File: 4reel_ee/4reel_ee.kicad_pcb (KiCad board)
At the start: 4 copper layers, 118 x 30 mm, 141 parts, among them J1 USB_C_Receptacle_USB2.0_16P, J2 Micro_SD_Card_Det2, J3 RJ45_Hanrun_HR911105A_Horizon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, J4 JST, U1 RV1103G, U2 EA3036C, U3 ImageSensor_OV9281, U4 TLV73312PDBV, U5 TPD2EUSB30, U6 TLV73328PDBV, U7 W25Q16JVSS, U8 LIS2HH12, U9 ImageSensor_OV9281, Y1 TXC-7C, Y2 24Mhz, Y3 TXC-7C

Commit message: Worked on the routing
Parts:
- removed R26, R27, R28, R29: 49.9R, Resistor_SMD:R_0402_1005Metric
- added C73: 10nF, Capacitor_SMD:C_0402_1005Metric, F.Cu at (110.5, 92.7)
- added C74: 10nF, Capacitor_SMD:C_0402_1005Metric, F.Cu at (109.1, 99.0)
- added C75: 100nF, Capacitor_SMD:C_0402_1005Metric, B.Cu at (124.2, 100.9)
- C17, C19, C21, C24, C27, C28, C37, C72: moved to B.Cu
- R16: moved to F.Cu
- U7: value W25Q16JVSS -> W25Q32JVZP; footprint Package_SO:SOIC-8_5.3x5.3mm_P1.27mm -> Package_SON:WSON-8-1EP_6x5mm_P1.27mm_EP3.4x4.3mm
- moved C54 115.5 mm to (119.0, 103.6), turned to 90 degrees
- moved C49 113.4 mm to (120.1, 103.6), turned to 90 degrees
- moved R22 110.3 mm to (122.2, 105.8), turned to 0 degrees
- moved U8 110.0 mm to (122.0, 104.0), turned to 180 degrees
- moved R21 108.7 mm to (122.2, 102.1), turned to 0 degrees
- moved U7 85.8 mm to (137.9, 106.2), turned to 180 degrees
- moved R30 60.1 mm to (107.9, 108.4), turned to 180 degrees
- moved R31 55.1 mm to (111.9, 108.4), turned to 0 degrees
- moved D1 28.4 mm to (118.2, 96.1), turned to 90 degrees
- moved D2 27.3 mm to (119.2, 96.1), turned to 90 degrees
- moved R23 26.7 mm to (118.2, 98.0), turned to -90 degrees
- moved R24 25.6 mm to (119.2, 98.0), turned to -90 degrees
- moved C72 9.78 mm to (122.5, 91.4), turned to 180 degrees
- moved C50 9.44 mm to (146.0, 96.8), turned to 0 degrees
- moved R11 8.89 mm to (108.7, 90.0)
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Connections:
- J3 pad 4: +3V3 -> Net-(J3-TCT)
- J3 pad 5: +3V3 -> Net-(J3-RCT)
- U1 pad 60: /MPU/STROBE1 -> /MPU/STROBE2
- U1 pad 61: /MPU/VSYNC1 -> /MPU/VSYNC2
- U1 pad 64: /MPU/XSHUTDOWN1 -> /MPU/XSHUTDOWN2
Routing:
- net +3V3: track 16.6 -> 139.4 mm, vias 1 -> 9
- net /MPU/I2C4.SDA: track 14.7 -> 81.9 mm, vias 0 -> 2
- net /MPU/I2C4.SCL: track 22.5 -> 89.7 mm, vias 0 -> 2
- net +5V: track 9.92 -> 58.0 mm
- net +1V8: track 8.95 -> 55.5 mm, vias 0 -> 6
- net /MPU/VSYNC2: track 0.69 -> 41.1 mm, vias 0 -> 1
- net /MPU/XSHUTDOWN2: track 2.39 -> 42.1 mm, vias 0 -> 1
- net /MPU/STROBE2: track 1.15 -> 40.5 mm, vias 0 -> 1
- net +0V9: track 0.00 -> 33.1 mm, vias 0 -> 6
- net /MPU/EPHY.RXN: track 0.00 -> 25.4 mm
- net /MPU/EPHY.RXP: track 0.00 -> 25.3 mm
- net /MPU/SDMMC.CLK: track 0.11 -> 23.7 mm, vias 0 -> 1
- net /MPU/EPHY.TXN: track 0.00 -> 23.4 mm
- net /MPU/EPHY.TXP: track 0.00 -> 23.2 mm
- net /Flash/FSPI.~{CS}: track 0.00 -> 21.6 mm, vias 0 -> 1
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
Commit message: Worked on the routing.
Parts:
- C35, C46, C58, C63, C67, C68, C71: moved to F.Cu
- moved C31 93.4 mm to (135.2, 110.0), turned to -90 degrees
- moved R18 90.2 mm to (134.0, 105.7), turned to 90 degrees
- moved R17 85.4 mm to (138.5, 103.0)
- moved C35 5.40 mm to (162.9, 95.7)
- moved C46 5.30 mm to (162.9, 94.7)
- moved C58 4.73 mm to (90.9, 94.4)
- moved C53 3.30 mm to (165.4, 91.2), turned to 90 degrees
- moved C63 3.02 mm to (90.9, 91.4), turned to 0 degrees
- moved R31 2.82 mm to (113.8, 110.5), turned to 90 degrees
- moved TP1 2.60 mm to (160.3, 107.4)
- moved TP2 2.55 mm to (157.8, 107.4)
- moved C66 2.24 mm to (88.9, 98.2), turned to -90 degrees
- moved C69 2.15 mm to (89.9, 98.2), turned to -90 degrees
- moved C71 2.14 mm to (90.9, 95.4)
- moved C48 1.58 mm to (166.8, 100.8), turned to 0 degrees
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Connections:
- J4 pad 2: /MPU/UART_RX -> /MPU/UART_TX
- J4 pad 3: /MPU/UART_TX -> /MPU/UART_RX
- U1 pad 52: unconnected-(U1GPIO / Peripherals-PWM10_M1-Pad52) -> /LED100
- U1 pad 57: unconnected-(U1GPIO / Peripherals-PWM3_IR_M2-Pad57) -> /LED_ACT
- U1 pad 61: /MPU/VSYNC2 -> /MPU/VSYNC
- U1 pad 64: /MPU/XSHUTDOWN2 -> /MPU/XSHUTDOWN
- U1 pad 65: unconnected-(U1GPIO / Peripherals-PWM2_M2-Pad65) -> /MPU/STROBE1
- U3 pad A5: /MPU/XSHUTDOWN1 -> /MPU/XSHUTDOWN
- U3 pad B5: /MPU/VSYNC1 -> /MPU/VSYNC
- U3 pad E1: +1V8 -> /OV9281/DVDD
- U9 pad A5: /MPU/XSHUTDOWN2 -> /MPU/XSHUTDOWN
- U9 pad B5: /MPU/VSYNC2 -> /MPU/VSYNC
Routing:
- net +1V8: track 55.5 -> 186.4 mm, vias 6 -> 11
- net +1V2: track 1.36 -> 125.5 mm, vias 0 -> 3
- net +2V8: track 4.51 -> 120.3 mm, vias 0 -> 4
- net /MPU/VSYNC: track 0.00 -> 91.5 mm, vias 0 -> 3
- net /MPU/XSHUTDOWN: track 0.00 -> 91.3 mm, vias 0 -> 1
- net +0V9: track 33.1 -> 100.4 mm, vias 6 -> 8
- net /MPU/STROBE1: track 2.19 -> 53.3 mm, vias 0 -> 1
- net /MPU/UART_TX: track 0.71 -> 44.8 mm, vias 1 -> 2
- net +5V: track 58.0 -> 100.4 mm, vias 2 -> 5
- net /MPU/XSHUTDOWN2: track 42.1 -> 0.00 mm, vias 1 -> 0
- net /MPU/UART_RX: track 0.77 -> 41.9 mm, vias 1 -> 2
- net /MPU/VSYNC2: track 41.1 -> 0.00 mm, vias 1 -> 0
- net +3V3: track 139.4 -> 180.1 mm, vias 9 -> 13
- net /LED_ACT: track 0.00 -> 27.8 mm, vias 0 -> 1
- net /LED100: track 0.00 -> 24.5 mm, vias 0 -> 1
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
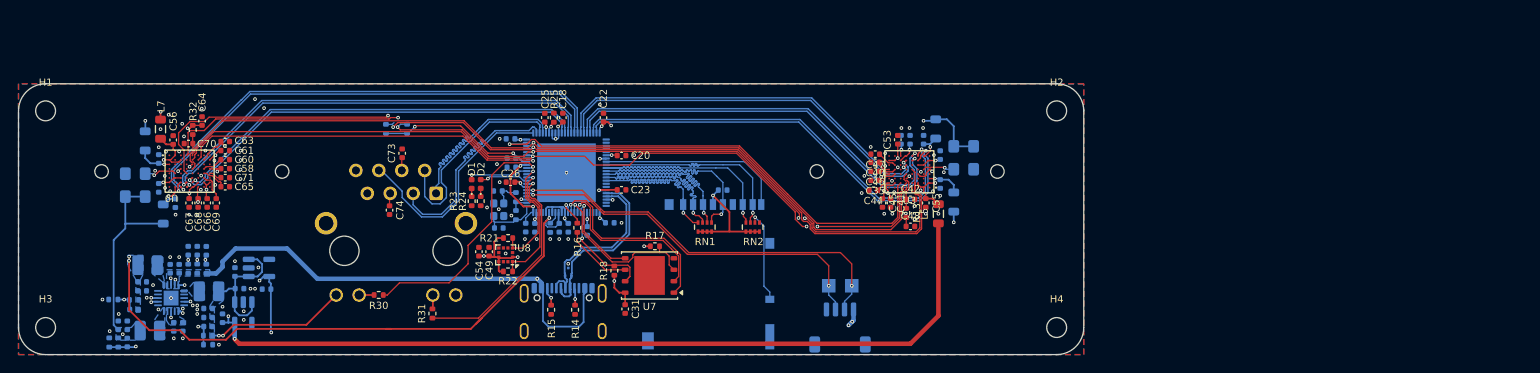
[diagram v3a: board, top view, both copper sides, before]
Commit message: Finished initial rough layout.
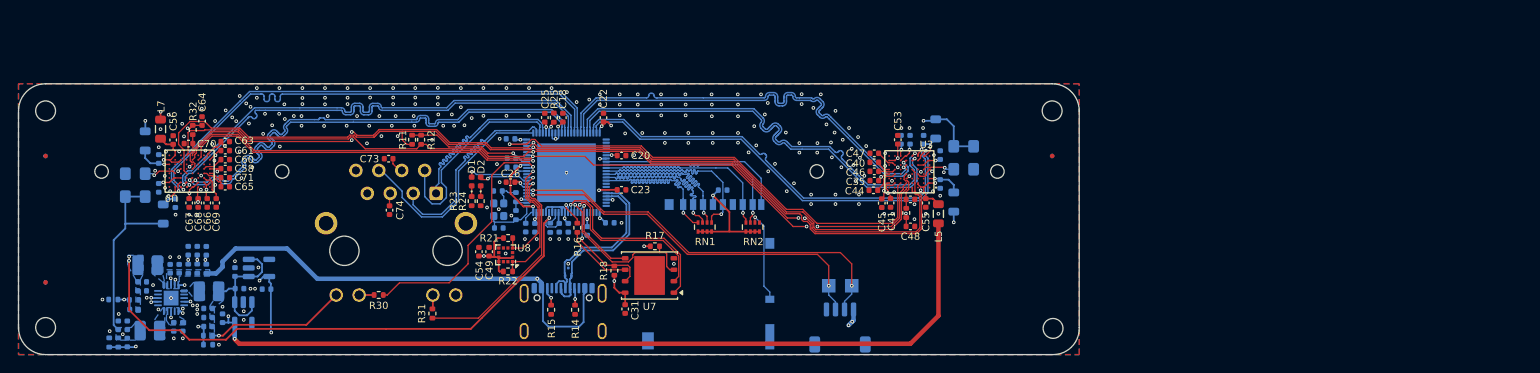
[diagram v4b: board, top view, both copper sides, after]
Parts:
- added FID1: Fiducial, Fiducial:Fiducial_0.5mm_Mask1.5mm, F.Cu at (71.0, 93.0)
- added FID2: Fiducial, Fiducial:Fiducial_0.5mm_Mask1.5mm, B.Cu at (71.0, 107.0)
- added FID3: Fiducial, Fiducial:Fiducial_0.5mm_Mask1.5mm, F.Cu at (71.0, 107.0)
- added FID4: Fiducial, Fiducial:Fiducial_0.5mm_Mask1.5mm, F.Cu at (182.5, 93.0)
- added FID5: Fiducial, Fiducial:Fiducial_0.5mm_Mask1.5mm, B.Cu at (71.0, 93.0)
- added FID6: Fiducial, Fiducial:Fiducial_0.5mm_Mask1.5mm, B.Cu at (182.5, 93.0)
- R11, R12: moved to F.Cu
- moved R11 3.14 mm to (111.6, 91.2), turned to -90 degrees
- moved R12 1.97 mm to (112.6, 91.2), turned to -90 degrees
- moved C73 1.62 mm to (109.0, 93.3), turned to 180 degrees
- moved H2 0.50 mm to (182.5, 88.0)
- moved H4 0.41 mm to (182.6, 112.1)
- moved D1 0.28 mm to (118.2, 95.8)
- moved D2 0.27 mm to (119.2, 95.8)
- moved C47 0.14 mm to (162.8, 92.7)
- moved C40 0.11 mm to (162.8, 93.7)
- moved C35 0.10 mm to (162.8, 95.7)
- moved C46 0.10 mm to (162.8, 94.7)
- moved C45 0.08 mm to (163.6, 98.2)
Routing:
- net /MPU/MIPI2.D1P: track 46.6 -> 53.2 mm
- net /MPU/MIPI2.D1N: track 46.9 -> 53.2 mm
- net /MPU/MIPI1.D1N: track 43.4 -> 47.9 mm
- net /MPU/MIPI1.D1P: track 44.0 -> 47.9 mm
- net +1V8: track 186.4 -> 182.7 mm, vias 11 -> 10
- net /MPU/MIPI2.CK0N: track 49.8 -> 53.3 mm
- net /MPU/MIPI1.CK0N: track 46.3 -> 49.4 mm
- net /MPU/I2C4.SDA: track 99.5 -> 96.6 mm, vias 5 -> 3
- net /MPU/MIPI1.CK0P: track 45.1 -> 48.0 mm
- net +3V3: track 180.1 -> 177.3 mm, vias 13 -> 11
- net /MPU/MIPI2.CK0P: track 50.9 -> 53.7 mm
- net +0V9: track 100.4 -> 98.2 mm
- net /MPU/VSYNC: track 91.5 -> 89.7 mm
- net /MPU/SDMMC.D0: track 24.5 -> 22.8 mm
- net /MPU/MIPI2.D0N: track 55.4 -> 56.6 mm
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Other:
- board size 118 x 30 mm -> 117.5 x 30 mm

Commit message: R0.1-rc1
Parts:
- added R26: 10k, Resistor_SMD:R_0402_1005Metric, F.Cu at (134.8, 96.3)
- added R27: 22R, Resistor_SMD:R_0201_0603Metric, B.Cu at (135.0, 94.4)
- moved C23 0.55 mm to (134.8, 97.3)
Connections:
- J2 pad 10: Net-(J2-DET_A) -> GND
- RN1 pad 1: /MPU/SDMMC.CLK -> unconnected-(RN1-R1.1-Pad1)
- RN2 pad 1: unconnected-(RN2-R1.1-Pad1) -> /MPU/SDMMC.DET
- RN2 pad 2: Net-(J2-DET_A) -> unconnected-(RN2-R2.1-Pad2)
- U1 pad 11: /MPU/SDMMC.CLK -> Net-(U1GPIO / Peripherals-SDMMC_CLK)
- U1 pad 16: unconnected-(U1Analog / High-Speed-SARADC_IN0-Pad16) -> Net-(U1Analog / High-Speed-SARADC_IN0)
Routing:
- net Net-(J2-DET_A): track 10.4 -> 0.00 mm, vias 1 -> 0
- net /MPU/MIPI2.D1P: track 53.2 -> 56.4 mm
- net /MPU/MIPI2.D1N: track 53.2 -> 56.4 mm
- net /MPU/MIPI2.CK0P: track 53.7 -> 56.9 mm
- net /MPU/MIPI2.CK0N: track 53.3 -> 56.5 mm
- net /MPU/SDMMC.CLK: track 23.7 -> 21.2 mm, vias 1 -> 0
- net /MPU/SDMMC.DET: track 20.8 -> 23.2 mm, vias 0 -> 1
- net Net-(U1GPIO / Peripherals-SDMMC_CLK): track 0.00 -> 1.69 mm
- net +1V8: track 182.7 -> 184.4 mm
- net /MPU/MIPI1.D1N: track 47.9 -> 49.3 mm
- net /MPU/MIPI1.D1P: track 47.9 -> 49.3 mm
- net /MPU/MIPI1.CK0P: track 48.0 -> 49.4 mm
- net Net-(U1Analog / High-Speed-SARADC_IN0): track 0.00 -> 1.24 mm, vias 0 -> 1
- net /MPU/MIPI1.D0P: track 48.1 -> 49.1 mm
- net /MPU/MIPI1.D0N: track 48.1 -> 49.2 mm
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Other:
- board text added: "100 OHM Controlled Impedance"
- board text added: "90 OHM Controlled impedance"

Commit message: R0.1 release.
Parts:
- added TP3: TestPoint, TestPoint:TestPoint_Pad_1.0x1.0mm, F.Cu at (110.1, 91.2)
- added TP4: TestPoint, TestPoint:TestPoint_Pad_1.0x1.0mm, F.Cu at (107.7, 91.7)
- added TP5: TestPoint, TestPoint:TestPoint_Pad_1.0x1.0mm, F.Cu at (124.3, 105.0)
- added TP6: TestPoint, TestPoint:TestPoint_Pad_1.0x1.0mm, F.Cu at (124.3, 103.0)
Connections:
- C35 pad 1: /OV9281/DOVDD -> /OV9281/DVDD
- C36 pad 1: /OV9281/DOVDD -> /OV9281/DVDD
- C39 pad 1: /OV9281/DVDD -> /OV9281/DOVDD
- C41 pad 1: /OV9281/DVDD -> /OV9281/DOVDD
- C51 pad 1: /OV9281/DVDD -> /OV9281/DOVDD
- C52 pad 1: /OV9281/DOVDD -> /OV9281/DVDD
- C55 pad 1: /OV9281/DOVDD -> /OV9281/DVDD
- C56 pad 1: /OV9282/DOVDD -> /OV9282/DVDD
- C58 pad 1: /OV9282/DOVDD -> /OV9282/DVDD
- C59 pad 1: /OV9282/DVDD -> /OV9282/DOVDD
- C62 pad 1: /OV9282/DOVDD -> /OV9282/DVDD
- C63 pad 1: /OV9282/DVDD -> /OV9282/DOVDD
- C67 pad 1: /OV9282/DOVDD -> /OV9282/DVDD
- C68 pad 1: /OV9282/DVDD -> /OV9282/DOVDD
- L5 pad 2: /OV9281/DOVDD -> /OV9281/DVDD
- L6 pad 2: /OV9281/DVDD -> /OV9281/DOVDD
- L7 pad 2: /OV9282/DOVDD -> /OV9282/DVDD
- L9 pad 2: /OV9282/DVDD -> /OV9282/DOVDD
- U3 pad A2: /OV9281/DOVDD -> /OV9281/DVDD
- U3 pad B1: /OV9281/DOVDD -> /OV9281/DVDD
- U3 pad B3: /OV9281/DOVDD -> /OV9281/DVDD
- U3 pad B7: /OV9281/DVDD -> /OV9281/DOVDD
- U3 pad C5: /OV9281/DOVDD -> /OV9281/DVDD
- U3 pad D3: /OV9281/DVDD -> /OV9281/DOVDD
- U3 pad D8: /OV9281/DOVDD -> /OV9281/DVDD
- U3 pad E1: /OV9281/DVDD -> /OV9281/DOVDD
- U3 pad F2: /OV9281/DOVDD -> /OV9281/DVDD
- U3 pad F3: /OV9281/DOVDD -> /OV9281/DVDD
- U3 pad G1: /OV9281/DOVDD -> /OV9281/DVDD
- U3 pad G6: /OV9281/DOVDD -> /OV9281/DVDD
- U3 pad H2: /OV9281/DVDD -> /OV9281/DOVDD
- U3 pad H5: /OV9281/DOVDD -> /OV9281/DVDD
- U3 pad H6: /OV9281/DVDD -> /OV9281/DOVDD
- U9 pad A2: /OV9282/DOVDD -> /OV9282/DVDD
- U9 pad B1: /OV9282/DOVDD -> /OV9282/DVDD
- U9 pad B3: /OV9282/DOVDD -> /OV9282/DVDD
- U9 pad B7: /OV9282/DVDD -> /OV9282/DOVDD
- U9 pad C5: /OV9282/DOVDD -> /OV9282/DVDD
- U9 pad D3: /OV9282/DVDD -> /OV9282/DOVDD
- U9 pad D8: /OV9282/DOVDD -> /OV9282/DVDD
- U9 pad F2: /OV9282/DOVDD -> /OV9282/DVDD
- U9 pad F3: /OV9282/DOVDD -> /OV9282/DVDD
- U9 pad G1: /OV9282/DOVDD -> /OV9282/DVDD
- U9 pad G6: /OV9282/DOVDD -> /OV9282/DVDD
- U9 pad H2: /OV9282/DVDD -> /OV9282/DOVDD
- U9 pad H5: /OV9282/DOVDD -> /OV9282/DVDD
- U9 pad H6: /OV9282/DVDD -> /OV9282/DOVDD
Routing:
- net /OV9282/DVDD: track 24.4 -> 27.7 mm, vias 4 -> 5
- net /OV9282/DOVDD: track 27.7 -> 24.5 mm, vias 5 -> 4
- net /OV9281/DVDD: track 24.8 -> 26.2 mm, vias 4 -> 5
- net /OV9281/DOVDD: track 26.2 -> 24.8 mm, vias 5 -> 4
- net /MPU/MIPI2.D0N: track 56.6 -> 55.9 mm
- net /MPU/MIPI2.D0P: track 56.7 -> 55.9 mm
- net /LED100: track 24.5 -> 25.3 mm
- net +0V9: track 98.2 -> 98.9 mm
